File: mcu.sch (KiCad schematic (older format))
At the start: 29 parts

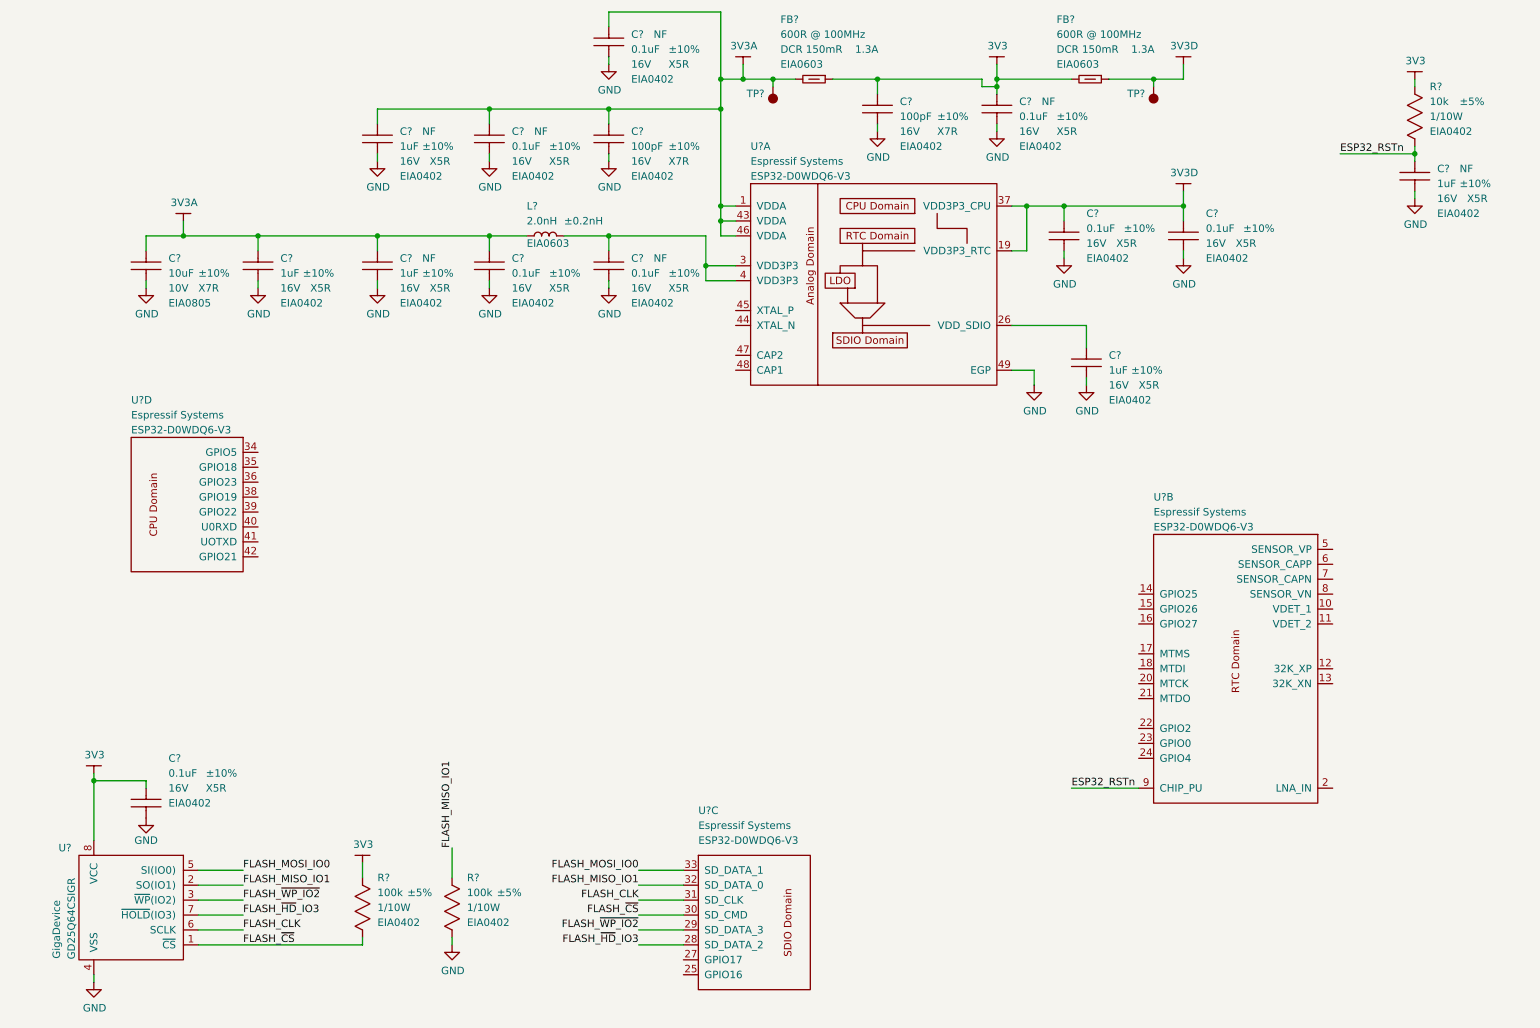
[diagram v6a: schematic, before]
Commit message: Add reset tact switch circuit.
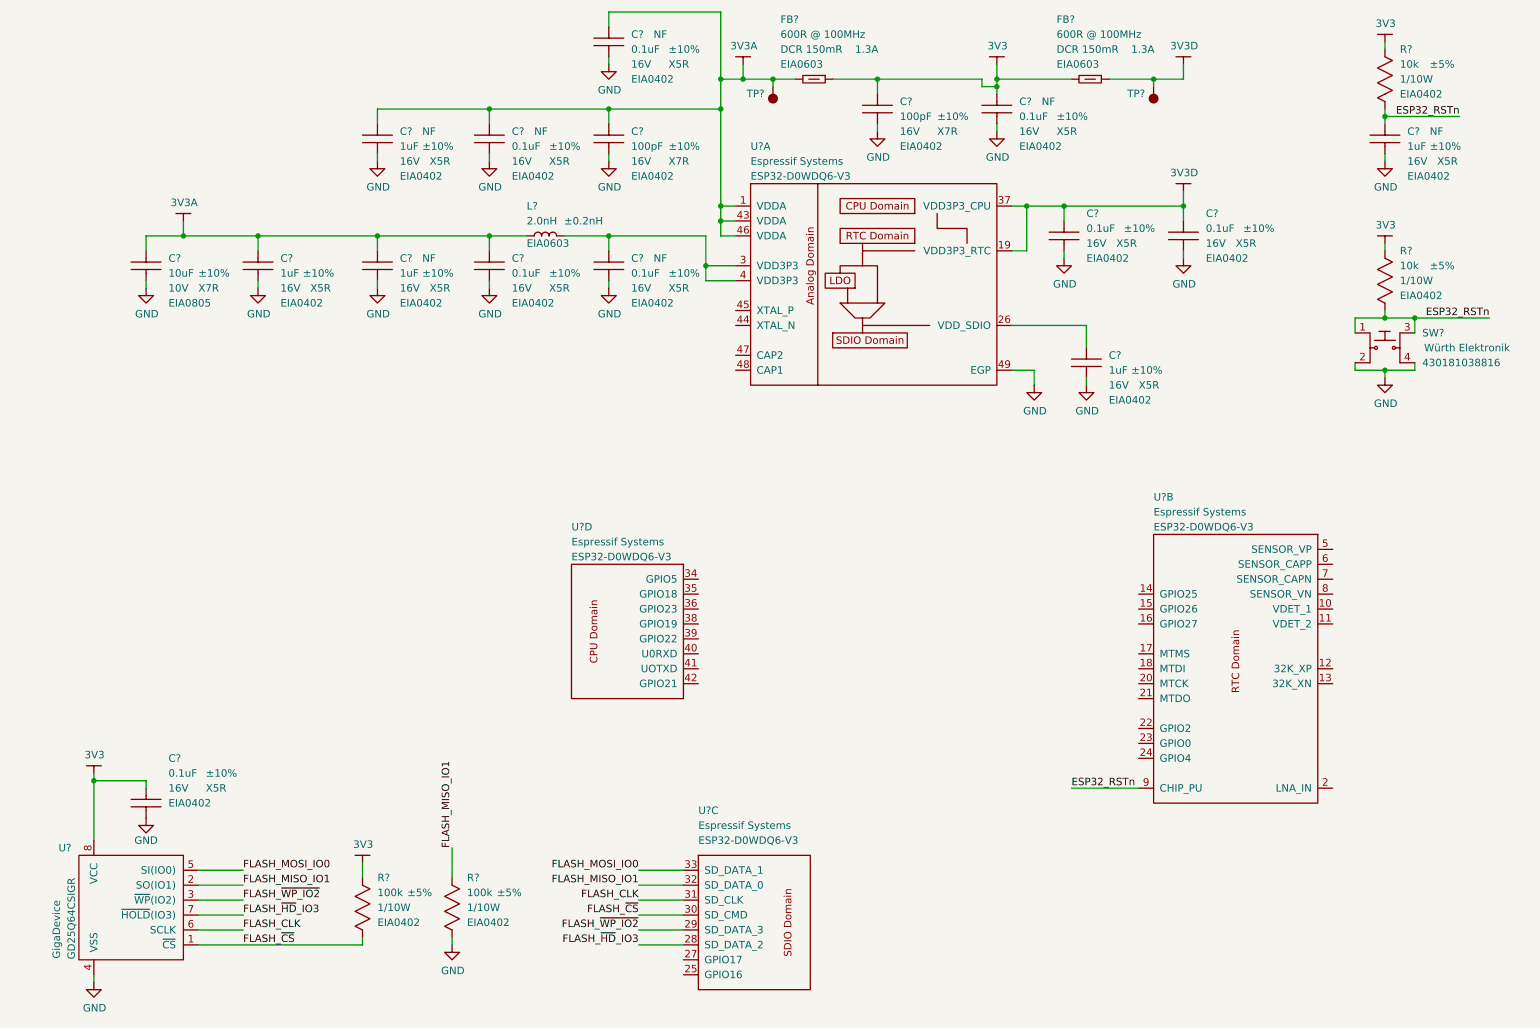
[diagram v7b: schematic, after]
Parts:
- added R?: RES-EIA0402, footprints_generic:RESC100X50X40L25NN, symbol gz_Chip-Resistors-Surface-Mount:RES-EIA0402
- added SW?: WE-430181038816, footprints:WE-430181038816_SWSOFL4P150_450X750X380L150X70N, symbol gz_Tactile-Switches:WE-430181038816
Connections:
- net +3V3: now also R?.1
- net ESP32_RSTn: now also R?.2, SW?.1, SW?.3
- net GND: now also SW?.2, SW?.4
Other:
- moved on the sheet: C?, R?, U?D
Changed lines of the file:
@@
 L gz_RF-Transceiver-ICs:Espressif_ESP32-D0WDQ6-V3 U?
 U 4 1 6050B3E7
-P 1950 4000
-F 0 "U?" H 1400 4650 50  0000 L CNN
-F 1 "Espressif_ESP32-D0WDQ6-V3" H 3700 5700 50  0001 L CNN
-F 2 "footprints:Espressif-ESP32_QFN49P40_600X600X90L40X20T430N" H 3700 5600 50  0001 L CNN
-F 3 "${DATASHEETS}/Espressif_ESP32-D0WDQ6-V3.pdf" H 3300 5300 50  0001 L CNN
-F 4 "1904-ESP32-D0WDQ6-V3CT-ND" H 4050 5500 50  0001 L CNN "Vendor_PN"
-F 5 "Espressif Systems" H 1400 4550 50  0000 L CNN "Manufacturer"
-F 6 "ESP32-D0WDQ6-V3" H 1400 4450 50  0000 L CNN "MPN"
-F 7 "RF/IF and RFID" H 3700 5400 50  0001 L CNN "Category"
-F 8 "RF Transceiver ICs" H 3700 5300 50  0001 L CNN "Family"
-F 9 "Yes" H 1700 4850 50  0001 L CNN "Fit"
-F 10 "Digikey" H 3700 5500 50  0001 L CNN "Vendor"
-	4    1950 4000
+P 4900 4850
+F 0 "U?" H 4350 5500 50  0000 L CNN
+F 1 "Espressif_ESP32-D0WDQ6-V3" H 6650 6550 50  0001 L CNN
+F 2 "footprints:Espressif-ESP32_QFN49P40_600X600X90L40X20T430N" H 6650 6450 50  0001 L CNN
+F 3 "${DATASHEETS}/Espressif_ESP32-D0WDQ6-V3.pdf" H 6250 6150 50  0001 L CNN
+F 4 "1904-ESP32-D0WDQ6-V3CT-ND" H 7000 6350 50  0001 L CNN "Vendor_PN"
+F 5 "Espressif Systems" H 4350 5400 50  0000 L CNN "Manufacturer"
+F 6 "ESP32-D0WDQ6-V3" H 4350 5300 50  0000 L CNN "MPN"
+F 7 "RF/IF and RFID" H 6650 6250 50  0001 L CNN "Category"
+F 8 "RF Transceiver ICs" H 6650 6150 50  0001 L CNN "Family"
+F 9 "Yes" H 4650 5700 50  0001 L CNN "Fit"
+F 10 "Digikey" H 6650 6350 50  0001 L CNN "Vendor"
+	4    4900 4850
 	1    0    0    -1
 $EndComp
@@
 L gz_Chip-Resistors-Surface-Mount:RES-EIA0402 R?
 U 1 1 605F571C
-P 10000 1450
-F 0 "R?" V 9800 1550 50  0000 L CNN
-F 1 "RES-EIA0402" H 10800 2350 50  0001 L CNN
-F 2 "footprints_generic:RESC100X50X40L25NN" H 6700 5800 50  0001 L CNN
-F 3 "${PANASONIC_GP_CHIP_RES_BASE}ERJ2GEJ103X" H 6700 5900 50  0001 L CNN
-F 4 "Digikey" H 10000 1450 50  0001 L CNN "Vendor"
-F 5 "P10KJCT-ND" H 10000 1450 50  0001 L CNN "Vendor_PN"
-F 6 "Panasonic Electronic Components" H 10800 2150 50  0001 L CNN "Manufacturer"
-F 7 "ERJ2GEJ103X" H 10800 2050 50  0001 L CNN "MPN"
-F 8 "Resistors" H 6700 6200 50  0001 L CNN "Category"
-F 9 "Chip Resistor - Surface Mount" H 6700 6300 50  0001 L CNN "Family"
-F 10 "Yes" H 10000 1450 50  0001 C CNN "Fit"
-F 11 "10k" V 9900 1550 50  0000 L CNN "Resistance"
-F 12 "±5%" V 9900 1750 50  0000 L CNN "Tolerance"
-F 13 "1/10W" V 10000 1550 50  0000 L CNN "Power"
-F 14 "N/A" H 10000 1665 50  0001 L CNN "Voltage"
-F 15 "EIA0402" V 10100 1550 50  0000 L CNN "Package"
-	1    10000 1450
+P 9800 1200
+F 0 "R?" V 9600 1300 50  0000 L CNN
+F 1 "RES-EIA0402" H 10600 2100 50  0001 L CNN
+F 2 "footprints_generic:RESC100X50X40L25NN" H 6500 5550 50  0001 L CNN
+F 3 "${PANASONIC_GP_CHIP_RES_BASE}ERJ2GEJ103X" H 6500 5650 50  0001 L CNN
+F 4 "Digikey" H 9800 1200 50  0001 L CNN "Vendor"
+F 5 "P10KJCT-ND" H 9800 1200 50  0001 L CNN "Vendor_PN"
+F 6 "Panasonic Electronic Components" H 10600 1900 50  0001 L CNN "Manufacturer"
+F 7 "ERJ2GEJ103X" H 10600 1800 50  0001 L CNN "MPN"
+F 8 "Resistors" H 6500 5950 50  0001 L CNN "Category"
+F 9 "Chip Resistor - Surface Mount" H 6500 6050 50  0001 L CNN "Family"
+F 10 "Yes" H 9800 1200 50  0001 C CNN "Fit"
+F 11 "10k" V 9700 1300 50  0000 L CNN "Resistance"
+F 12 "±5%" V 9700 1500 50  0000 L CNN "Tolerance"
+F 13 "1/10W" V 9800 1300 50  0000 L CNN "Power"
+F 14 "N/A" H 9800 1415 50  0001 L CNN "Voltage"
+F 15 "EIA0402" V 9900 1300 50  0000 L CNN "Package"
+	1    9800 1200
 	0    1    1    0
 $EndComp
@@
 L gz_Ceramic-Capacitors:CAP-EIA0402 C?
 U 1 1 605F9AA8
-P 10000 1850
-F 0 "C?" V 9950 2000 50  0000 L CNN
-F 1 "CAP-EIA0402" H 10400 2950 50  0001 L CNN
-F 2 "footprints_generic:CAPC100X50X55L30N" H 6700 6200 50  0001 L CNN
-F 3 "${KEMET_MLCC_BASE}C0402C105K4PACTU" H 6700 6300 50  0001 L CNN
-F 4 "Digikey" H 10000 1850 50  0001 L CNN "Vendor"
-F 5 "399-12289-1-ND" H 10000 1850 50  0001 L CNN "Vendor_PN"
-F 6 "KEMET" H 10400 2750 50  0001 L CNN "Manufacturer"
-F 7 "C0402C105K4PACTU" H 10400 2650 50  0001 L CNN "MPN"
-F 8 "Capacitors" H 6700 6600 50  0001 L CNN "Category"
-F 9 "Ceramic Capacitors" H 6700 6700 50  0001 L CNN "Family"
-F 10 "NF" V 9950 2150 50  0000 L CNN "Fit"
-F 11 "1uF" V 10050 2000 50  0000 L CNN "Capacitance"
-F 12 "±10%" V 10050 2150 50  0000 L CNN "Tolerance"
-F 13 "16V" V 10150 2000 50  0000 L CNN "Voltage"
-F 14 "X5R" V 10150 2200 50  0000 L CNN "Dielectric"
-F 15 "EIA0402" V 10250 2000 50  0000 L CNN "Package"
-	1    10000 1850
+P 9800 1600
+F 0 "C?" V 9750 1750 50  0000 L CNN
+F 1 "CAP-EIA0402" H 10200 2700 50  0001 L CNN
+F 2 "footprints_generic:CAPC100X50X55L30N" H 6500 5950 50  0001 L CNN
+F 3 "${KEMET_MLCC_BASE}C0402C105K4PACTU" H 6500 6050 50  0001 L CNN
+F 4 "Digikey" H 9800 1600 50  0001 L CNN "Vendor"
+F 5 "399-12289-1-ND" H 9800 1600 50  0001 L CNN "Vendor_PN"
+F 6 "KEMET" H 10200 2500 50  0001 L CNN "Manufacturer"
+F 7 "C0402C105K4PACTU" H 10200 2400 50  0001 L CNN "MPN"
+F 8 "Capacitors" H 6500 6350 50  0001 L CNN "Category"
+F 9 "Ceramic Capacitors" H 6500 6450 50  0001 L CNN "Family"
+F 10 "NF" V 9750 1900 50  0000 L CNN "Fit"
+F 11 "1uF" V 9850 1750 50  0000 L CNN "Capacitance"
+F 12 "±10%" V 9850 1900 50  0000 L CNN "Tolerance"
+F 13 "16V" V 9950 1750 50  0000 L CNN "Voltage"
+F 14 "X5R" V 9950 1950 50  0000 L CNN "Dielectric"
+F 15 "EIA0402" V 10050 1750 50  0000 L CNN "Package"
+	1    9800 1600
 	0    1    1    0
 $EndComp
@@
 L gz_Power-Symbols:GND #PWR?
 U 1 1 60607E38
-P 10000 2000
-F 0 "#PWR?" H 10000 1750 50  0001 C CNN
-F 1 "GND" H 10005 1827 50  0000 C CNN
-F 2 "" H 10000 2000 50  0001 C CNN
-F 3 "" H 10000 2000 50  0001 C CNN
-	1    10000 2000
+P 9800 1750
+F 0 "#PWR?" H 9800 1500 50  0001 C CNN
+F 1 "GND" H 9805 1577 50  0000 C CNN
+F 2 "" H 9800 1750 50  0001 C CNN
+F 3 "" H 9800 1750 50  0001 C CNN
+	1    9800 1750
 	1    0    0    -1
 $EndComp
@@
 L gz_Power-Symbols:3V3 #PWR?
 U 1 1 606086F3
-P 10000 1200
-F 0 "#PWR?" H 10150 1150 50  0001 C CNN
-F 1 "3V3" H 10005 1323 50  0000 C CNN
-F 2 "" H 10000 1200 50  0001 C CNN
-F 3 "" H 10000 1200 50  0001 C CNN
-	1    10000 1200
-	1    0    0    -1
-$EndComp
-Wire Wire Line
-	10000 1200 10000 1250
-Wire Wire Line
-	10000 1650 10000 1700
-Wire Wire Line
-	10000 1950 10000 2000
-Wire Wire Line
-	10000 1700 9500 1700
-Connection ~ 10000 1700
-Wire Wire Line
-	10000 1700 10000 1750
-Text Label 9500 1700 0    50   ~ 0
+P 9800 950
+F 0 "#PWR?" H 9950 900 50  0001 C CNN
+F 1 "3V3" H 9805 1073 50  0000 C CNN
+F 2 "" H 9800 950 50  0001 C CNN
+F 3 "" H 9800 950 50  0001 C CNN
+	1    9800 950
+	1    0    0    -1
+$EndComp
+Wire Wire Line
+	9800 950  9800 1000
+Wire Wire Line
+	9800 1400 9800 1450
+Wire Wire Line
+	9800 1700 9800 1750
+Connection ~ 9800 1450
+Wire Wire Line
+	9800 1450 9800 1500
+Text Label 10300 1450 2    50   ~ 0
 ESP32_RSTn
 Wire Wire Line
@@
 Text Label 7700 5950 0    50   ~ 0
 ESP32_RSTn
+$Comp
+L gz_Tactile-Switches:WE-430181038816 SW?
+U 1 1 6063C7C1
+P 9800 3000
+F 0 "SW?" H 10050 3100 50  0000 L CNN
+F 1 "WE-430181038816" H 10450 3700 50  0001 L CNN
+F 2 "footprints:WE-430181038816_SWSOFL4P150_450X750X380L150X70N" H 10450 3600 50  0001 L CNN
+F 3 "https://katalog.we-online.de/em/datasheet/430181038816.pdf" H 10000 3300 50  0001 L CNN
+F 4 "Digikey" H 10450 3500 50  0001 L CNN "Vendor"
+F 5 "732-7003-1-ND" H 10850 3500 50  0001 L CNN "Vendor_PN"
+F 6 "Würth Elektronik" H 10350 3000 50  0000 C CNN "Manufacturer"
+F 7 "430181038816" H 10050 2900 50  0000 L CNN "MPN"
+F 8 "Switches" H 10450 3400 50  0001 L CNN "Category"
+F 9 "Tactile Switches" H 10450 3300 50  0001 L CNN "Family"
+F 10 "Yes" H 9950 3250 50  0001 L CNN "Fit"
+	1    9800 3000
+	1    0    0    -1
+$EndComp
+Wire Wire Line
+	9600 3100 9600 3150
+Wire Wire Line
+	10000 3150 10000 3100
+$Comp
+L gz_Power-Symbols:GND #PWR?
+U 1 1 60648C32
+P 9800 3200
+F 0 "#PWR?" H 9800 2950 50  0001 C CNN
+F 1 "GND" H 9805 3027 50  0000 C CNN
+F 2 "" H 9800 3200 50  0001 C CNN
+F 3 "" H 9800 3200 50  0001 C CNN
+	1    9800 3200
+	1    0    0    -1
+$EndComp
+$Comp
+L gz_Chip-Resistors-Surface-Mount:RES-EIA0402 R?
+U 1 1 6064D1F7
+P 9800 2550
+F 0 "R?" V 9600 2650 50  0000 L CNN
+F 1 "RES-EIA0402" H 10600 3450 50  0001 L CNN
+F 2 "footprints_generic:RESC100X50X40L25NN" H 6500 6900 50  0001 L CNN
+F 3 "${PANASONIC_GP_CHIP_RES_BASE}ERJ2GEJ103X" H 6500 7000 50  0001 L CNN
+F 4 "Digikey" H 9800 2550 50  0001 L CNN "Vendor"
+F 5 "P10KJCT-ND" H 9800 2550 50  0001 L CNN "Vendor_PN"
+F 6 "Panasonic Electronic Components" H 10600 3250 50  0001 L CNN "Manufacturer"
+F 7 "ERJ2GEJ103X" H 10600 3150 50  0001 L CNN "MPN"
+F 8 "Resistors" H 6500 7300 50  0001 L CNN "Category"
+F 9 "Chip Resistor - Surface Mount" H 6500 7400 50  0001 L CNN "Family"
+F 10 "Yes" H 9800 2550 50  0001 C CNN "Fit"
+F 11 "10k" V 9700 2650 50  0000 L CNN "Resistance"
+F 12 "±5%" V 9700 2850 50  0000 L CNN "Tolerance"
+F 13 "1/10W" V 9800 2650 50  0000 L CNN "Power"
+F 14 "N/A" H 9800 2765 50  0001 L CNN "Voltage"
+F 15 "EIA0402" V 9900 2650 50  0000 L CNN "Package"
+	1    9800 2550
+	0    1    1    0
+$EndComp
+Wire Wire Line
+	9600 2900 9600 2800
+Wire Wire Line
+	10000 2800 10000 2900
+Text Label 10500 2800 2    50   ~ 0
+ESP32_RSTn
+Wire Wire Line
+	9600 2800 9800 2800
+Wire Wire Line
+	9800 2800 9800 2750
+Connection ~ 9800 2800
+Wire Wire Line
+	9800 2800 10000 2800
+Wire Wire Line
+	9800 2300 9800 2350
+$Comp
+L gz_Power-Symbols:3V3 #PWR?
+U 1 1 6065ADB6
+P 9800 2300
+F 0 "#PWR?" H 9950 2250 50  0001 C CNN
+F 1 "3V3" H 9805 2423 50  0000 C CNN
+F 2 "" H 9800 2300 50  0001 C CNN
+F 3 "" H 9800 2300 50  0001 C CNN
+	1    9800 2300
+	1    0    0    -1
+$EndComp
+Wire Wire Line
+	9600 3150 9800 3150
+Wire Wire Line
+	9800 3150 9800 3200
+Connection ~ 9800 3150
+Wire Wire Line
+	9800 3150 10000 3150
+Connection ~ 10000 2800
+Wire Wire Line
+	10000 2800 10500 2800
+Wire Wire Line
+	9800 1450 10300 1450
 $EndSCHEMATC

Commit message: Add HF XTAL circuit.
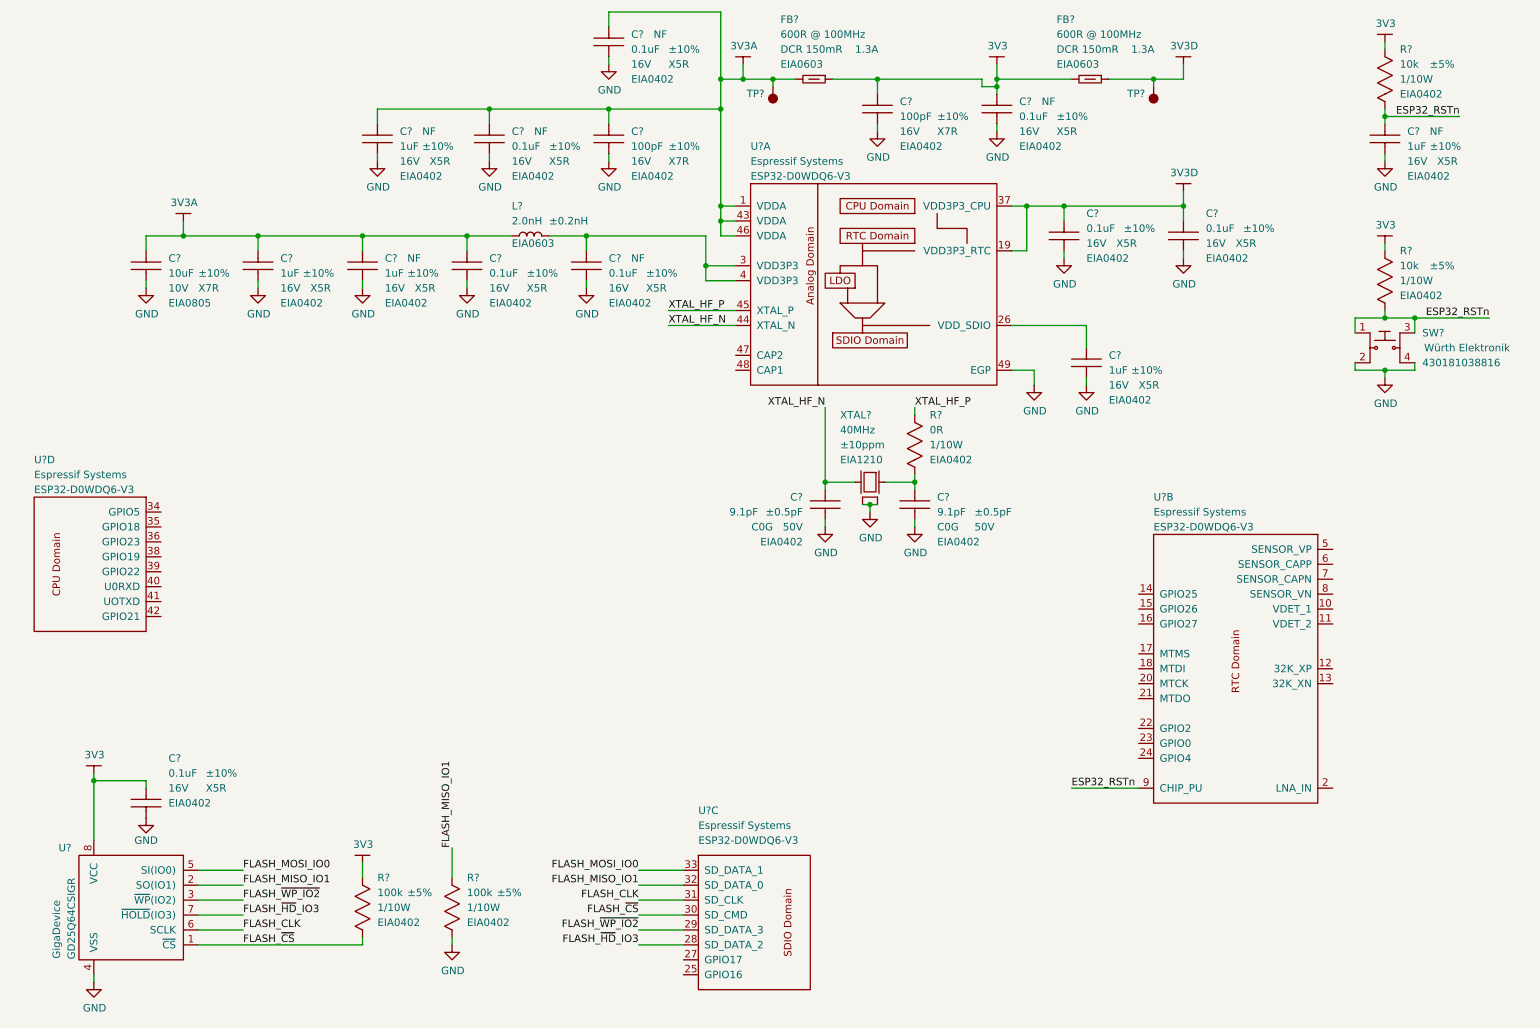
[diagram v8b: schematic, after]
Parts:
- added C? (x2): CAP-EIA0402, footprints_generic:CAPC100X50X55L30N, symbol gz_Ceramic-Capacitors:CAP-EIA0402
- added R?: RES-EIA0402, footprints_generic:RESC100X50X40L25NN, symbol gz_Chip-Resistors-Surface-Mount:RES-EIA0402
- added XTAL?: RaltronElectronics-RH100-40.000-9-F-1010-EXT-TR, footprints:RaltronElectronics-RH100_XTALDFN4_250X320X80L90X100N, symbol gz_Crystals:RaltronElectronics-RH100-40.000-9-F-1010-EXT-TR
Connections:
- net GND: now also C?.2, C?.2, XTAL?.2, XTAL?.4
- net XTAL_HF_N: now reaches U?.44 (XTAL_N)
- net XTAL_HF_N: now also C?.1, XTAL?.1
- net XTAL_HF_P: now reaches U?.45 (XTAL_P)
- net XTAL_HF_P: now also R?.1
- new net: C?.1, R?.2, XTAL?.3
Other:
- moved on the sheet: C?, L?, U?D
